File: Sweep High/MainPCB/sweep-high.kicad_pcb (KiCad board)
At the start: 2 copper layers, 229.5 x 95.2 mm, 61 parts, among them J1 AudioJack4dpb, J2 AudioJack4dpb, SW10 SW_Push, SW10_r1 SW_Push, SW11 SW_Push, SW11_r1 SW_Push, SW12 SW_Push, SW12_r1 SW_Push, SW13_r1 SW_Push, SW14 SW_Push, SW14_r1 SW_Push, SW15 SW_Push, SW15_r1 SW_Push, SW16 SW_Push, SW16_r1 SW_Push, SW17 SW_Push, SW17_r1 SW_Push, SW18 SW_Push, SW18_r1 SW_Push, SW2 SW_Push, SW20 SW_Push, SW21 SW_Push, SW2_r1 SW_Push, SW3 SW_Push, SW3_r1 SW_Push, SW4 SW_Push, SW4_r1 SW_Push, SW5 SW_Push, SW5_r1 SW_Push, SW6 SW_Push, SW6_r1 SW_Push, SW7_r1 SW_Push, SW8 SW_Push, SW8_r1 SW_Push, SW9 SW_Push, SW9_r1 SW_Push, U1 ProMicro-kbd, U2 ProMicro-kbd

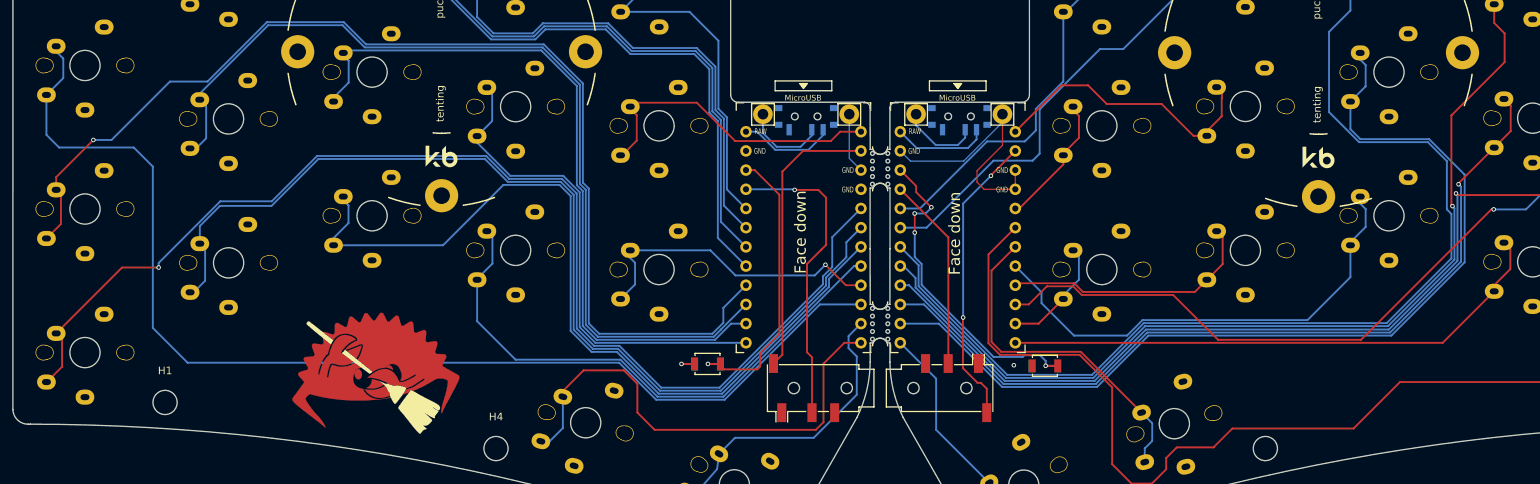
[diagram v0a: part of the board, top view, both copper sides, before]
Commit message: some adjustments and stuff, changed my mind on some footprints and also missed some stuff I used for alignment and checking
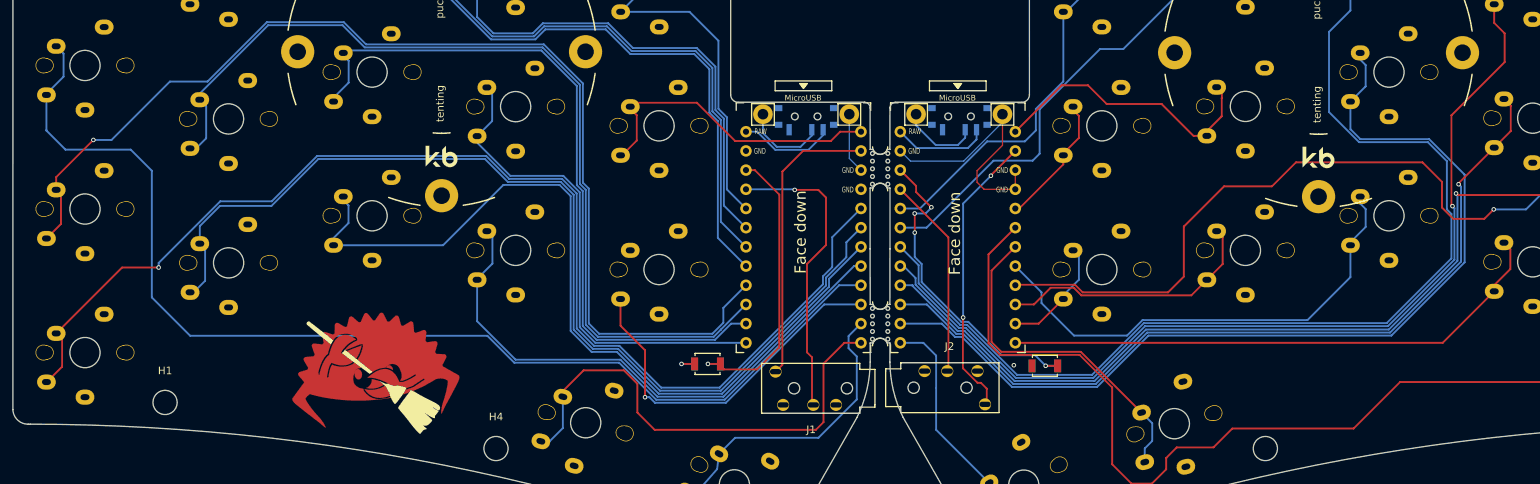
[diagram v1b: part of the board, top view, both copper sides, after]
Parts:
- J1, J2: footprint Connector_Audio:Jack_3.5mm_PJ320D_Horizontal -> env_extra:PJ-320A
- moved J1 8.79 mm to (149.6, 121.9)
- moved J2 8.75 mm to (151.0, 117.5)
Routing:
- net Switch15: track 41.1 -> 48.6 mm
- net Switch1_r: track 107.6 -> 113.6 mm
- net Switch1: track 153.1 -> 151.2 mm
- net Switch9_r: track 30.6 -> 32.4 mm
- net Switch18_r: track 39.1 -> 38.1 mm
- net Switch18: track 37.4 -> 38.4 mm
- net Switch15_r: track 34.2 -> 35.2 mm
- net reset_r: track 43.7 -> 42.9 mm
